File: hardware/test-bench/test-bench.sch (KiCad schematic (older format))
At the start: 36 parts, among them J1 Conn_Mem_Ext, J2 Conn_Reg, J3 SWD, J4 Conn_Mem, J5 FTDI, J6 Conn_Power, SW1 SW_Push_4pin, SW2 SW_Push_4pin, U1 STM32G030F6, U2 MCP23S17_SS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

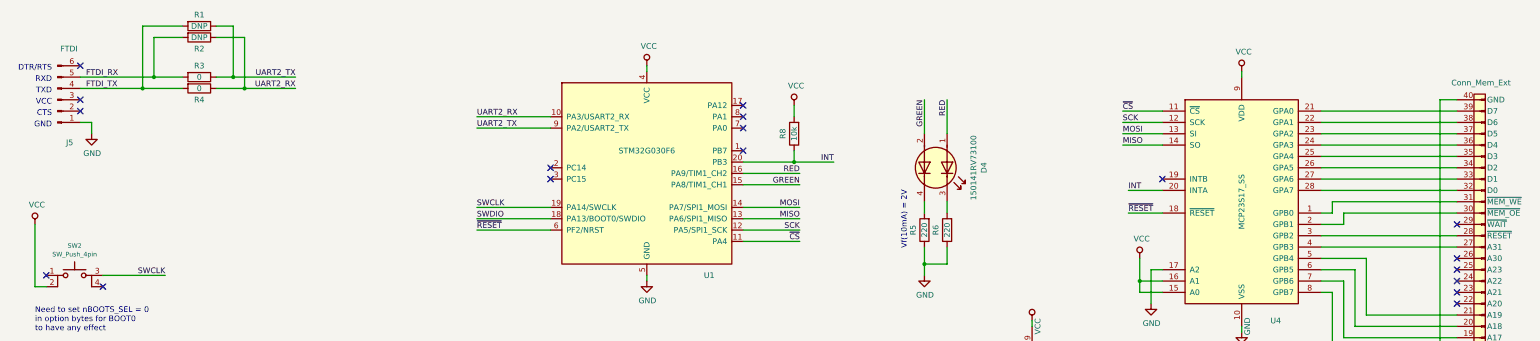
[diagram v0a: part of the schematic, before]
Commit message: Added ~RESET to memory bus
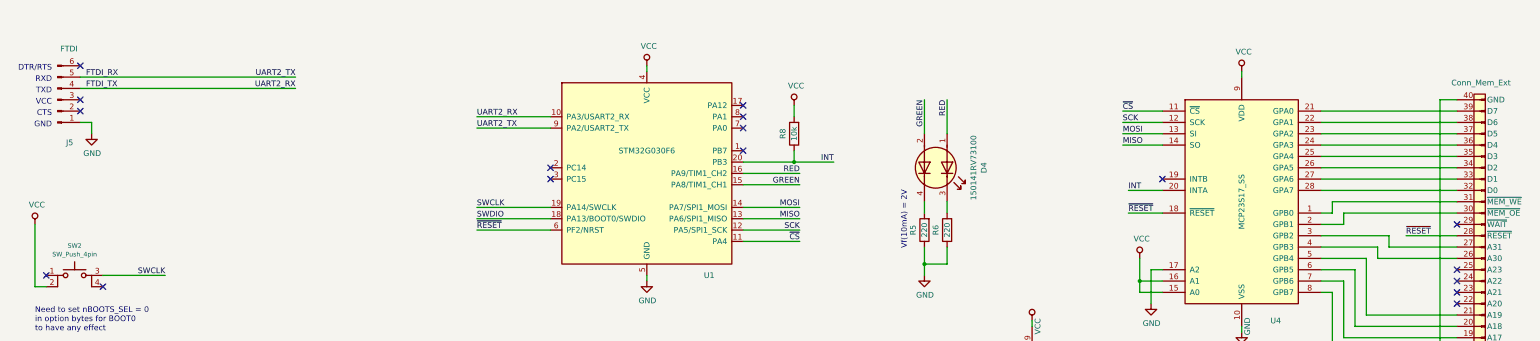
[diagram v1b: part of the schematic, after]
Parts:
- removed R1, R2: DNP, Resistor_SMD:R_0805_2012Metric, symbol Device:R
- removed R3, R4: 0, Resistor_SMD:R_0805_2012Metric, symbol Device:R
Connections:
- net UART2_RX is gone; now on net FTDI_TX: U1.10 (PA3/USART2_RX)
- net UART2_TX is gone; now on net FTDI_RX: U1.9 (PA2/USART2_TX)
- net ~RESET: now also J1.28 (~RESET)
- net at J1.26 (A30): now also U4.4 (GPB3)
- net at J1.27 (A31): now also U4.3 (GPB2); no longer U4.4 (GPB3)
- no-connect marks 25 -> 24
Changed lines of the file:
@@
 	14150 3400 14950 3400
-Wire Wire Line
-	13750 2800 14950 2800
-Wire Wire Line
-	13750 2700 14950 2700
 Wire Wire Line
 	13750 2200 14950 2200
@@
 NoConn ~ 2800 1600
 NoConn ~ 2800 1500
-$Comp
-L Device:R R1
-U 1 1 5F47700B
-P 3850 850
-F 0 "R1" V 3750 850 50  0000 C CNN
-F 1 "DNP" V 3850 850 50  0000 C CNN
-F 2 "Resistor_SMD:R_0805_2012Metric" V 3780 850 50  0001 C CNN
-F 3 "~" H 3850 850 50  0001 C CNN
-	1    3850 850
-	0    1    1    0
-$EndComp
-$Comp
-L Device:R R2
-U 1 1 5F47FE06
-P 3850 950
-F 0 "R2" V 3950 950 50  0000 C CNN
-F 1 "DNP" V 3850 950 50  0000 C CNN
-F 2 "Resistor_SMD:R_0805_2012Metric" V 3780 950 50  0001 C CNN
-F 3 "~" H 3850 950 50  0001 C CNN
-	1    3850 950
-	0    1    1    0
-$EndComp
-$Comp
-L Device:R R3
-U 1 1 5F47FE40
-P 3850 1300
-F 0 "R3" V 3750 1300 50  0000 C CNN
-F 1 "0" V 3850 1300 50  0000 C CNN
-F 2 "Resistor_SMD:R_0805_2012Metric" V 3780 1300 50  0001 C CNN
-F 3 "~" H 3850 1300 50  0001 C CNN
-	1    3850 1300
-	0    1    1    0
-$EndComp
-$Comp
-L Device:R R4
-U 1 1 5F47FE80
-P 3850 1400
-F 0 "R4" V 3950 1400 50  0000 C CNN
-F 1 "0" V 3850 1400 50  0000 C CNN
-F 2 "Resistor_SMD:R_0805_2012Metric" V 3780 1400 50  0001 C CNN
-F 3 "~" H 3850 1400 50  0001 C CNN
-	1    3850 1400
-	0    1    1    0
-$EndComp
-Wire Wire Line
-	2800 1400 3350 1400
-Wire Wire Line
-	3700 1300 3450 1300
-Wire Wire Line
-	3350 1400 3350 850
-Wire Wire Line
-	3350 850  3700 850
-Connection ~ 3350 1400
-Wire Wire Line
-	3350 1400 3700 1400
-Wire Wire Line
-	3700 950  3450 950
-Wire Wire Line
-	3450 950  3450 1300
-Connection ~ 3450 1300
-Wire Wire Line
-	3450 1300 2800 1300
-Wire Wire Line
-	4000 950  4250 950
-Wire Wire Line
-	4250 950  4250 1400
-Wire Wire Line
-	4250 1400 4000 1400
-Wire Wire Line
-	4000 1300 4150 1300
-Wire Wire Line
-	4150 1300 4150 850
-Wire Wire Line
-	4150 850  4000 850
 Text Label 4700 1400 2    50   ~ 0
 UART2_RX
-Wire Wire Line
-	4700 1400 4250 1400
-Connection ~ 4250 1400
 Text Label 4700 1300 2    50   ~ 0
 UART2_TX
-Wire Wire Line
-	4700 1300 4150 1300
-Connection ~ 4150 1300
 $Comp
 L power:GND #PWR01
@@
 NoConn ~ 8650 1550
 NoConn ~ 14950 2600
-NoConn ~ 14950 2900
 NoConn ~ 14950 3000
 NoConn ~ 14950 3100
@@
 Wire Wire Line
 	9100 1550 9100 1650
+Wire Wire Line
+	2800 1300 4700 1300
+Wire Wire Line
+	2800 1400 4700 1400
+Wire Wire Line
+	13750 2800 14250 2800
+Wire Wire Line
+	14250 2800 14250 2900
+Wire Wire Line
+	14250 2900 14950 2900
+Wire Wire Line
+	13750 2700 14350 2700
+Wire Wire Line
+	14350 2700 14350 2800
+Wire Wire Line
+	14350 2800 14950 2800
+Text Label 14500 2700 0    50   ~ 0
+~RESET
+Wire Wire Line
+	14500 2700 14950 2700
 $EndSCHEMATC

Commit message: Unified footprints
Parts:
- C1, C2, C3, C4, C5, C6, C7, C8: footprint Capacitor_SMD:C_0805_2012Metric -> Capacitor_SMD:C_0805_2012Metric_Pad1.15x1.40mm_HandSolder
- R5, R6, R7, R8: footprint Resistor_SMD:R_0805_2012Metric -> Resistor_SMD:R_0805_2012Metric_Pad1.15x1.40mm_HandSolder
- U6: footprint Package_TO_SOT_SMD:SOT-23-5 -> Package_TO_SOT_SMD:SOT-23-5_HandSoldering
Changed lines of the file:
@@
 F 0 "U6" H 10450 7867 50  0000 C CNN
 F 1 "MIC5504-3.3YM5" H 10450 7776 50  0000 C CNN
-F 2 "Package_TO_SOT_SMD:SOT-23-5" H 10450 7100 50  0001 C CNN
+F 2 "Package_TO_SOT_SMD:SOT-23-5_HandSoldering" H 10450 7100 50  0001 C CNN
 F 3 "http://ww1.microchip.com/downloads/en/DeviceDoc/MIC550X.pdf" H 10200 7750 50  0001 C CNN
 	1    10450 7500
@@
 F 0 "C1" H 9765 7696 50  0000 L CNN
 F 1 "1u" H 9765 7605 50  0000 L CNN
-F 2 "Capacitor_SMD:C_0805_2012Metric" H 9688 7500 50  0001 C CNN
+F 2 "Capacitor_SMD:C_0805_2012Metric_Pad1.15x1.40mm_HandSolder" H 9688 7500 50  0001 C CNN
 F 3 "~" H 9650 7650 50  0001 C CNN
 	1    9650 7650
@@
 F 0 "C2" H 11115 7696 50  0000 L CNN
 F 1 "1u" H 11115 7605 50  0000 L CNN
-F 2 "Capacitor_SMD:C_0805_2012Metric" H 11038 7500 50  0001 C CNN
+F 2 "Capacitor_SMD:C_0805_2012Metric_Pad1.15x1.40mm_HandSolder" H 11038 7500 50  0001 C CNN
 F 3 "~" H 11000 7650 50  0001 C CNN
 	1    11000 7650
@@
 F 0 "R7" V 11800 7800 50  0000 C CNN
 F 1 "330" V 11700 7800 50  0000 C CNN
-F 2 "Resistor_SMD:R_0805_2012Metric" V 11630 7800 50  0001 C CNN
+F 2 "Resistor_SMD:R_0805_2012Metric_Pad1.15x1.40mm_HandSolder" V 11630 7800 50  0001 C CNN
 F 3 "~" H 11700 7800 50  0001 C CNN
 	1    11700 7800
@@
 F 0 "R5" V 10350 2650 50  0000 C CNN
 F 1 "220" V 10250 2650 50  0000 C CNN
-F 2 "Resistor_SMD:R_0805_2012Metric" V 10180 2650 50  0001 C CNN
+F 2 "Resistor_SMD:R_0805_2012Metric_Pad1.15x1.40mm_HandSolder" V 10180 2650 50  0001 C CNN
 F 3 "~" H 10250 2650 50  0001 C CNN
 	1    10250 2650
@@
 F 0 "R6" V 10550 2650 50  0000 C CNN
 F 1 "220" V 10450 2650 50  0000 C CNN
-F 2 "Resistor_SMD:R_0805_2012Metric" V 10380 2650 50  0001 C CNN
+F 2 "Resistor_SMD:R_0805_2012Metric_Pad1.15x1.40mm_HandSolder" V 10380 2650 50  0001 C CNN
 F 3 "~" H 10450 2650 50  0001 C CNN
 	1    10450 2650
@@
 F 0 "C3" H 1715 3446 50  0000 L CNN
 F 1 "100n" H 1715 3355 50  0000 L CNN
-F 2 "Capacitor_SMD:C_0805_2012Metric" H 1638 3250 50  0001 C CNN
+F 2 "Capacitor_SMD:C_0805_2012Metric_Pad1.15x1.40mm_HandSolder" H 1638 3250 50  0001 C CNN
 F 3 "~" H 1600 3400 50  0001 C CNN
 	1    1600 3400
@@
 F 0 "C4" H 9615 9146 50  0000 L CNN
 F 1 "100n" H 9615 9055 50  0000 L CNN
-F 2 "Capacitor_SMD:C_0805_2012Metric" H 9538 8950 50  0001 C CNN
+F 2 "Capacitor_SMD:C_0805_2012Metric_Pad1.15x1.40mm_HandSolder" H 9538 8950 50  0001 C CNN
 F 3 "~" H 9500 9100 50  0001 C CNN
 	1    9500 9100
@@
 F 0 "C5" H 10065 9146 50  0000 L CNN
 F 1 "100n" H 10065 9055 50  0000 L CNN
-F 2 "Capacitor_SMD:C_0805_2012Metric" H 9988 8950 50  0001 C CNN
+F 2 "Capacitor_SMD:C_0805_2012Metric_Pad1.15x1.40mm_HandSolder" H 9988 8950 50  0001 C CNN
 F 3 "~" H 9950 9100 50  0001 C CNN
 	1    9950 9100
@@
 F 0 "C6" H 10515 9146 50  0000 L CNN
 F 1 "100n" H 10515 9055 50  0000 L CNN
-F 2 "Capacitor_SMD:C_0805_2012Metric" H 10438 8950 50  0001 C CNN
+F 2 "Capacitor_SMD:C_0805_2012Metric_Pad1.15x1.40mm_HandSolder" H 10438 8950 50  0001 C CNN
 F 3 "~" H 10400 9100 50  0001 C CNN
 	1    10400 9100
@@
 F 0 "C7" H 10965 9146 50  0000 L CNN
 F 1 "100n" H 10965 9055 50  0000 L CNN
-F 2 "Capacitor_SMD:C_0805_2012Metric" H 10888 8950 50  0001 C CNN
+F 2 "Capacitor_SMD:C_0805_2012Metric_Pad1.15x1.40mm_HandSolder" H 10888 8950 50  0001 C CNN
 F 3 "~" H 10850 9100 50  0001 C CNN
 	1    10850 9100
@@
 F 0 "C8" H 11415 9146 50  0000 L CNN
 F 1 "100n" H 11415 9055 50  0000 L CNN
-F 2 "Capacitor_SMD:C_0805_2012Metric" H 11338 8950 50  0001 C CNN
+F 2 "Capacitor_SMD:C_0805_2012Metric_Pad1.15x1.40mm_HandSolder" H 11338 8950 50  0001 C CNN
 F 3 "~" H 11300 9100 50  0001 C CNN
 	1    11300 9100
@@
 F 0 "R8" V 9200 1800 50  0000 C CNN
 F 1 "10k" V 9100 1800 50  0000 C CNN
-F 2 "Resistor_SMD:R_0805_2012Metric" V 9030 1800 50  0001 C CNN
+F 2 "Resistor_SMD:R_0805_2012Metric_Pad1.15x1.40mm_HandSolder" V 9030 1800 50  0001 C CNN
 F 3 "~" H 9100 1800 50  0001 C CNN
 	1    9100 1800

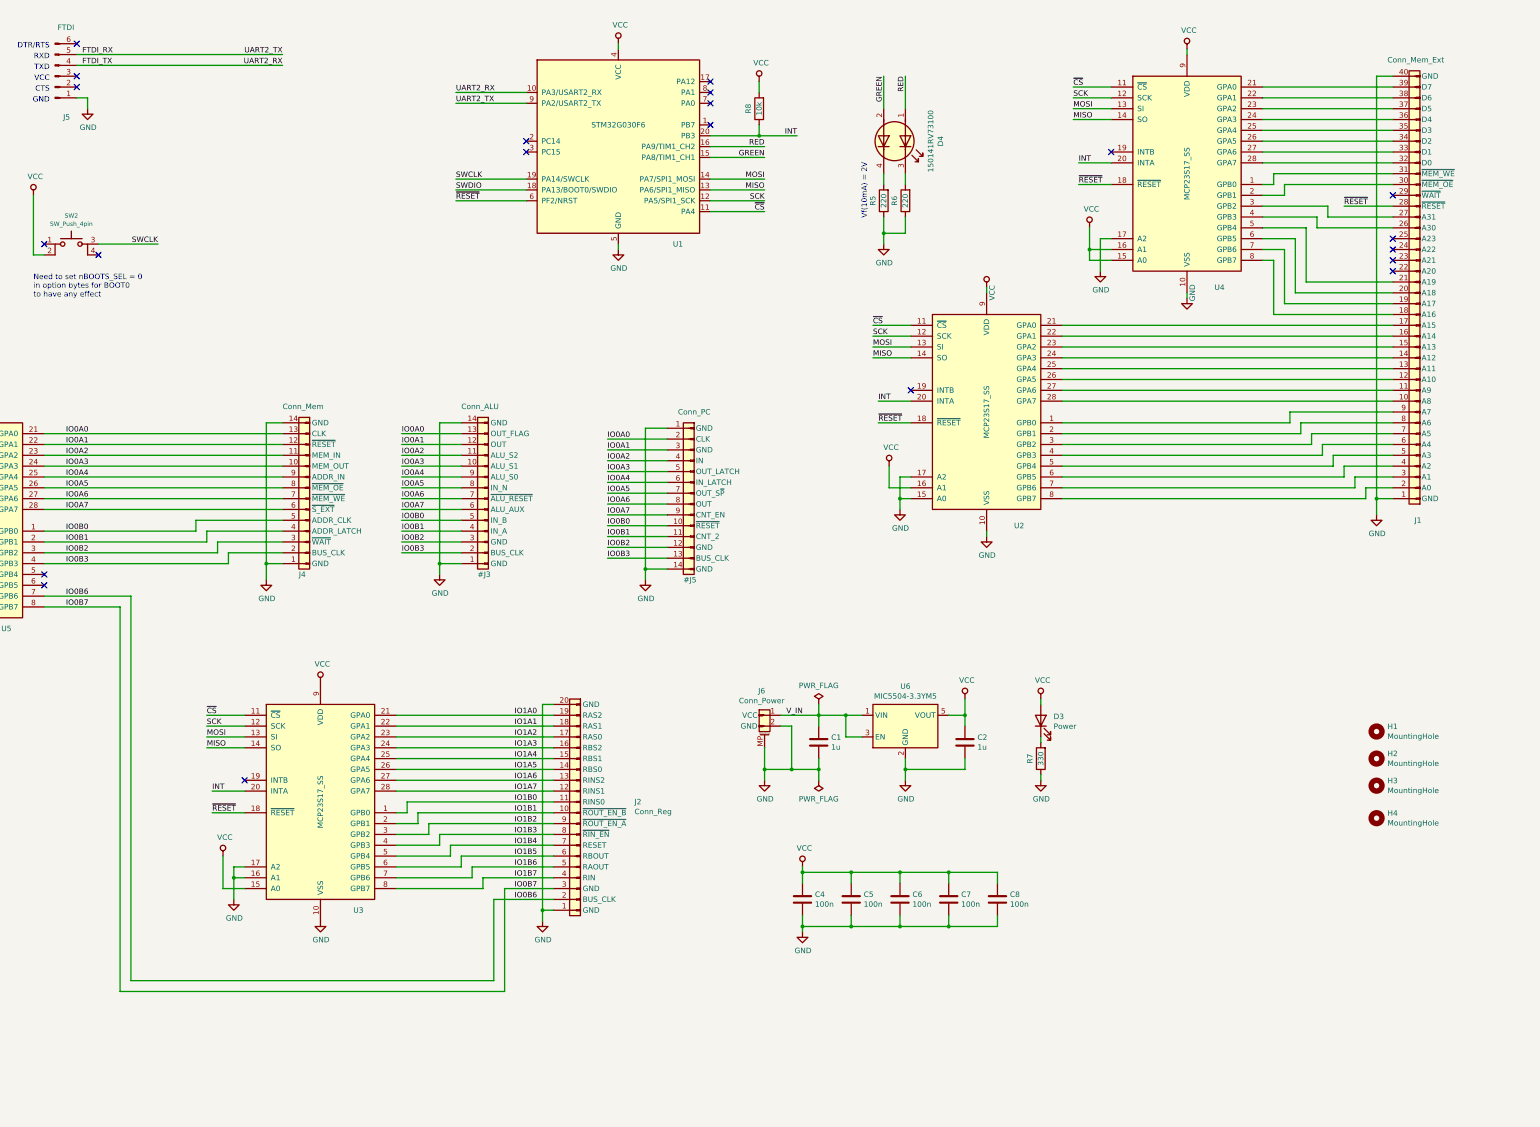
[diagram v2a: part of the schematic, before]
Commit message: Fully connect test headers
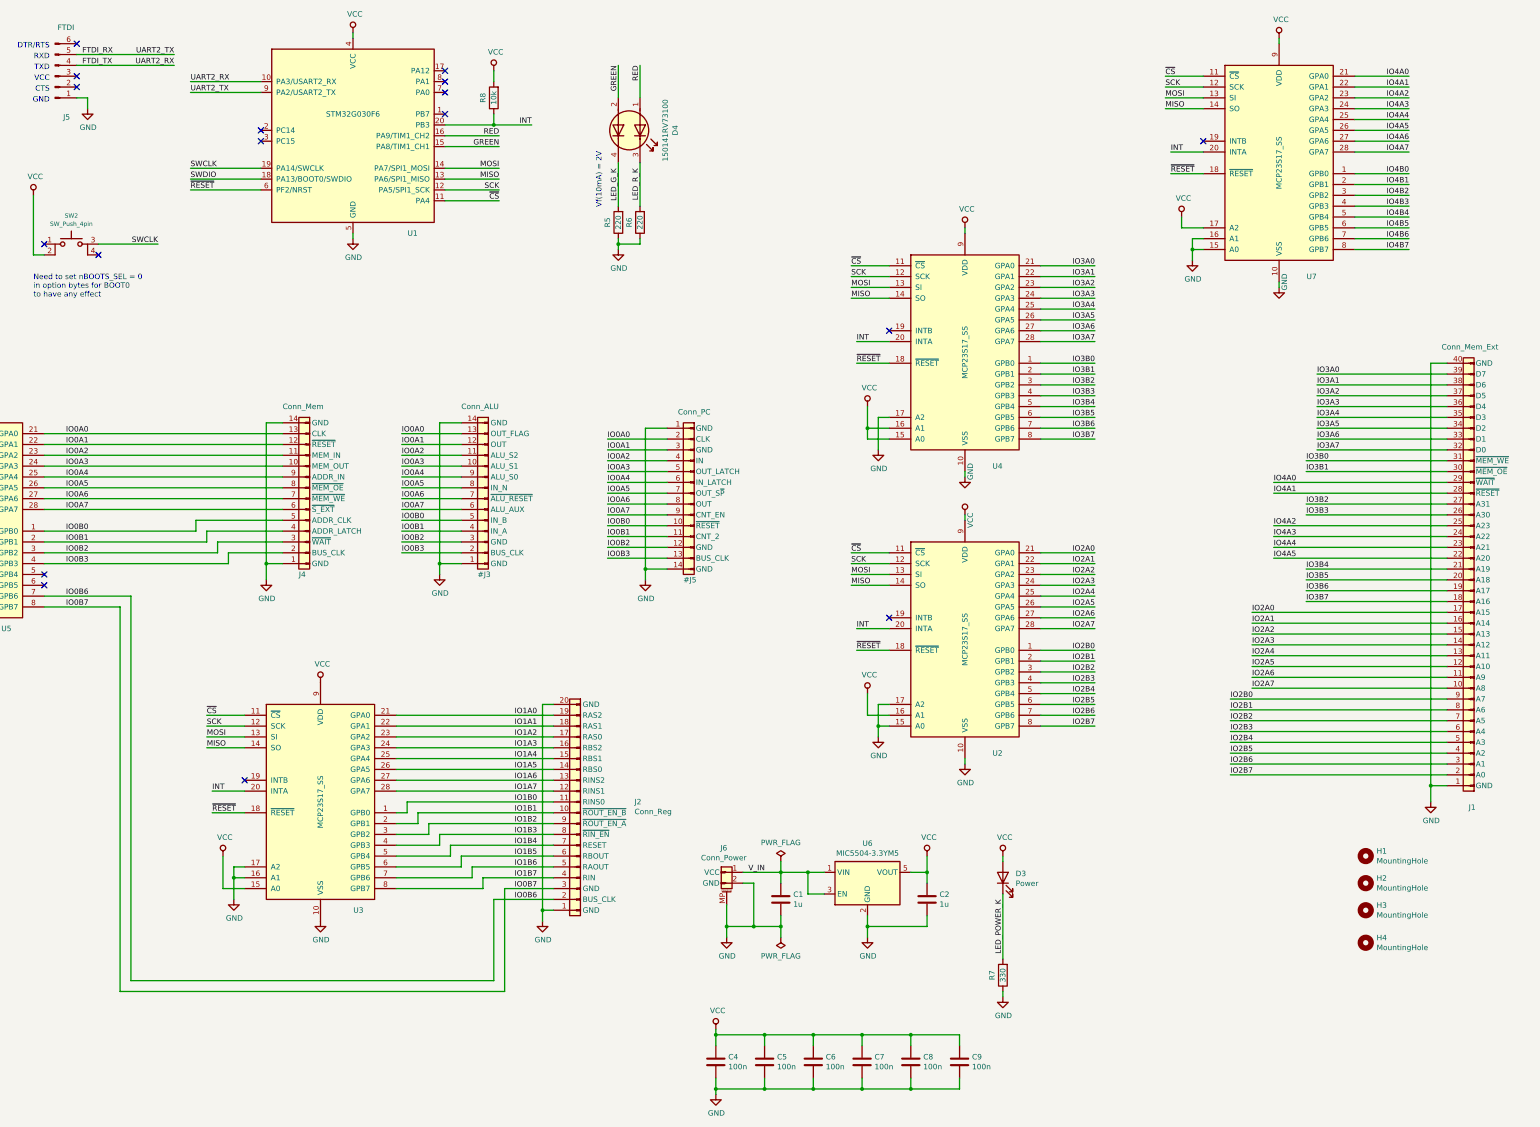
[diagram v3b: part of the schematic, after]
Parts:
- added C9: 100n, Capacitor_SMD:C_0805_2012Metric_Pad1.15x1.40mm_HandSolder, symbol Device:C
- added U7: MCP23S17_SS, Package_SO:SSOP-28_5.3x10.2mm_P0.65mm, symbol riscv-serial:MCP23S17_SS
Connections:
- net GND: now also C9.2, U7.10 (VSS), U7.15 (A0), U7.16 (A1)
- net INT: now also U7.20 (INTA)
- net MISO: now also U7.14 (SO)
- net MOSI: now also U7.13 (SI)
- net SCK: now also U7.12 (SCK)
- net VCC: now also C9.1, U7.17 (A2), U7.9 (VDD)
- net ~CS: now also U7.11 (~CS~)
- net ~RESET: now also U7.18 (~RESET~); no longer J1.28 (~RESET)
- net IO2A7: now reaches J1.10 (A8), U2.28 (GPA7)
- net IO2A6: now reaches J1.11 (A9), U2.27 (GPA6)
- net IO2A5: now reaches J1.12 (A10), U2.26 (GPA5)
- net IO2A4: now reaches J1.13 (A11), U2.25 (GPA4)
- net IO2A3: now reaches J1.14 (A12), U2.24 (GPA3)
- net IO2A2: now reaches J1.15 (A13), U2.23 (GPA2)
- net IO2A1: now reaches J1.16 (A14), U2.22 (GPA1)
- net IO2A0: now reaches J1.17 (A15), U2.21 (GPA0)
- net IO3B7: now reaches J1.18 (A16), U4.8 (GPB7)
- net IO3B6: now reaches J1.19 (A17), U4.7 (GPB6)
- net IO2B7: now reaches J1.2 (A0), U2.8 (GPB7)
- net IO3B5: now reaches J1.20 (A18), U4.6 (GPB5)
- net IO3B4: now reaches J1.21 (A19), U4.5 (GPB4)
- net IO4A5: now reaches J1.22 (A20)
- net IO4A5: now also U7.26 (GPA5)
- net IO4A4: now reaches J1.23 (A21)
- net IO4A4: now also U7.25 (GPA4)
- net IO4A3: now reaches J1.24 (A22)
- net IO4A3: now also U7.24 (GPA3)
- net IO4A2: now reaches J1.25 (A23)
- net IO4A2: now also U7.23 (GPA2)
- net IO3B3: now reaches J1.26 (A30), U4.4 (GPB3)
- net IO3B2: now reaches J1.27 (A31), U4.3 (GPB2)
- net IO4A0: now reaches J1.29 (~WAIT)
- net IO4A0: now also U7.21 (GPA0)
- net IO2B6: now reaches J1.3 (A1), U2.7 (GPB6)
- net IO3B1: now reaches J1.30 (~MEM_OE), U4.2 (GPB1)
- net IO3B0: now reaches J1.31 (~MEM_WE), U4.1 (GPB0)
- net IO3A7: now reaches J1.32 (D0), U4.28 (GPA7)
- net IO3A6: now reaches J1.33 (D1), U4.27 (GPA6)
- net IO3A5: now reaches J1.34 (D2), U4.26 (GPA5)
- net IO3A4: now reaches J1.35 (D3), U4.25 (GPA4)
- net IO3A3: now reaches J1.36 (D4), U4.24 (GPA3)
- net IO3A2: now reaches J1.37 (D5), U4.23 (GPA2)
- net IO3A1: now reaches J1.38 (D6), U4.22 (GPA1)
- net IO3A0: now reaches J1.39 (D7), U4.21 (GPA0)
- net IO2B5: now reaches J1.4 (A2), U2.6 (GPB5)
- net IO2B4: now reaches J1.5 (A3), U2.5 (GPB4)
- net IO2B3: now reaches J1.6 (A4), U2.4 (GPB3)
- net IO2B2: now reaches J1.7 (A5), U2.3 (GPB2)
- net IO2B1: now reaches J1.8 (A6), U2.2 (GPB1)
- net IO2B0: now reaches J1.9 (A7), U2.1 (GPB0)
- net LED_POWER_K: now reaches D3.1 (K), R7.2
- net LED_R_K: now reaches D4.3 (K1), R6.2
- net LED_G_K: now reaches D4.4 (K2), R5.2
- new net IO4A1: J1.28 (~RESET), U7.22 (GPA1)
- new net IO4A6: U7.27 (GPA6)
- new net IO4A7: U7.28 (GPA7)
- new net IO4B0: U7.1 (GPB0)
- new net IO4B1: U7.2 (GPB1)
- new net IO4B2: U7.3 (GPB2)
- new net IO4B3: U7.4 (GPB3)
- new net IO4B4: U7.5 (GPB4)
- new net IO4B5: U7.6 (GPB5)
- new net IO4B6: U7.7 (GPB6)
- new net IO4B7: U7.8 (GPB7)
- no-connect marks 24 -> 20
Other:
- moved on the sheet: C1, C2, C4, C5, C6, C7, C8, D3, D4, H1, H2, H3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
